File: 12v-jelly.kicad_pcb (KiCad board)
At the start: 4 copper layers, 46 x 68 mm, 30 parts, among them J1 PWR, J10 8, J3 1, J4 2, J5 3, J6 4, J7 5, J8 6, J9 7, Q1 DMP2022LSS-13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

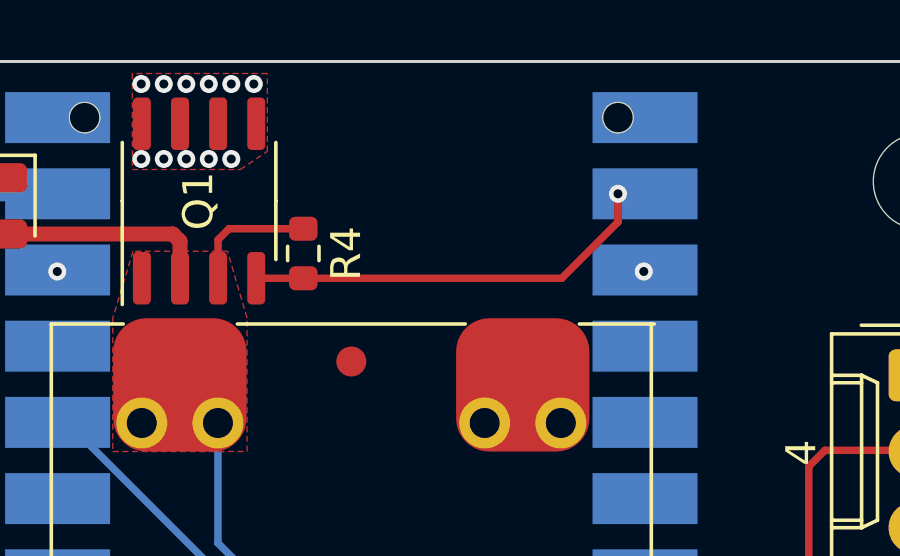
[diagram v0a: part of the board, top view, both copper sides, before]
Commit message: Driver NMOS
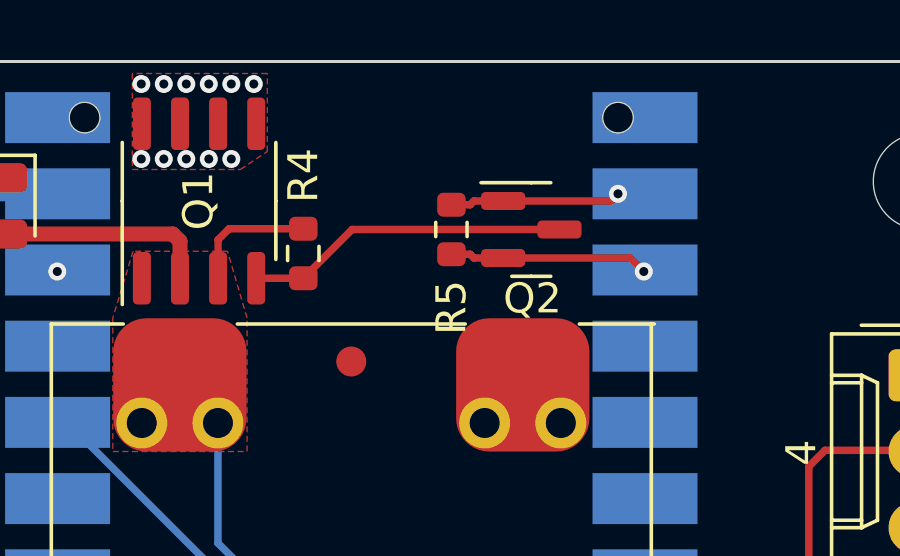
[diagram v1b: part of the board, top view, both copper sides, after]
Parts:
- added Q2: 2N7002, Package_TO_SOT_SMD:SOT-23, F.Cu at (86.0, 25.6)
- added R5: 10k, Resistor_SMD:R_0603_1608Metric, F.Cu at (83.3, 25.6)
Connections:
- Q1 pad 4: /LED_EN -> Net-(Q1-G)
- R4 pad 2: /LED_EN -> Net-(Q1-G)
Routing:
- net Net-(Q1-G): track 0.00 -> 10.8 mm
- net /LED_EN: track 13.8 -> 5.70 mm
- net GND: track 14.4 -> 21.0 mm
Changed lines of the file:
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@@
   (net 50 "/LED_EN")
   (net 51 "unconnected-(U2-GPIO0-Pad1)")
+  (net 52 "Net-(Q1-G)")
+  (footprint "Package_TO_SOT_SMD:SOT-23" (layer "F.Cu")
+    (at 86 25.6)
+    (descr "SOT, 3 Pin (https://www.jedec.org/system/files/docs/to-236h.pdf variant AB), generated with kicad-footprint-generator ipc_gullwing_generator.py")
+    (tags "SOT TO_SOT_SMD")
+    (property "Sheetfile" "12v-jelly.kicad_sch")
+    (property "Sheetname" "")
+    (property "ki_description" "0.115A Id, 60V Vds, N-Channel MOSFET, SOT-23")
+    (property "ki_keywords" "N-Channel Switching MOSFET")
+    (attr smd)
+    (fp_text reference "Q2" (at 0.0375 2.3) (layer "F.SilkS")
+        (effects (font (size 1 1) (thickness 0.15)))
+    )
+    (fp_text value "2N7002" (at 0 2.4) (layer "F.Fab")
+        (effects (font (size 1 1) (thickness 0.15)))
+    )
+    (fp_text user "${REFERENCE}" (at 0 0) (layer "F.Fab")
+        (effects (font (size 0.32 0.32) (thickness 0.05)))
+    )
+    (fp_line (start 0 -1.56) (end -1.675 -1.56)
+      (stroke (width 0.12) (type solid)) (layer "F.SilkS"))
+    (fp_line (start 0 -1.56) (end 0.65 -1.56)
+      (stroke (width 0.12) (type solid)) (layer "F.SilkS"))
+    (fp_line (start 0 1.56) (end -0.65 1.56)
+      (stroke (width 0.12) (type solid)) (layer "F.SilkS"))
+    (fp_line (start 0 1.56) (end 0.65 1.56)
+      (stroke (width 0.12) (type solid)) (layer "F.SilkS"))
+    (fp_line (start -1.92 -1.7) (end -1.92 1.7)
+      (stroke (width 0.05) (type solid)) (layer "F.CrtYd"))
+    (fp_line (start -1.92 1.7) (end 1.92 1.7)
+      (stroke (width 0.05) (type solid)) (layer "F.CrtYd"))
+    (fp_line (start 1.92 -1.7) (end -1.92 -1.7)
+      (stroke (width 0.05) (type solid)) (layer "F.CrtYd"))
+    (fp_line (start 1.92 1.7) (end 1.92 -1.7)
+      (stroke (width 0.05) (type solid)) (layer "F.CrtYd"))
+    (fp_line (start -0.65 -1.125) (end -0.325 -1.45)
+      (stroke (width 0.1) (type solid)) (layer "F.Fab"))
+    (fp_line (start -0.65 1.45) (end -0.65 -1.125)
+      (stroke (width 0.1) (type solid)) (layer "F.Fab"))
+    (fp_line (start -0.325 -1.45) (end 0.65 -1.45)
+      (stroke (width 0.1) (type solid)) (layer "F.Fab"))
+    (fp_line (start 0.65 -1.45) (end 0.65 1.45)
+      (stroke (width 0.1) (type solid)) (layer "F.Fab"))
+    (fp_line (start 0.65 1.45) (end -0.65 1.45)
+      (stroke (width 0.1) (type solid)) (layer "F.Fab"))
+    (pad "1" smd roundrect (at -0.9375 -0.95) (size 1.475 0.6) (layers "F.Cu" "F.Paste" "F.Mask") (roundrect_rratio 0.25)
+      (net 50 "/LED_EN") (pinfunction "G") (pintype "input"))
+    (pad "2" smd roundrect (at -0.9375 0.95) (size 1.475 0.6) (layers "F.Cu" "F.Paste" "F.Mask") (roundrect_rratio 0.25)
+      (net 2 "GND") (pinfunction "S") (pintype "passive"))
+    (pad "3" smd roundrect (at 0.9375 0) (size 1.475 0.6) (layers "F.Cu" "F.Paste" "F.Mask") (roundrect_rratio 0.25)
+      (net 52 "Net-(Q1-G)") (pinfunction "D") (pintype "passive"))
+    (model "${KICAD6_3DMODEL_DIR}/Package_TO_SOT_SMD.3dshapes/SOT-23.wrl"
+      (offset (xyz 0 0 0))
+      (scale (xyz 1 1 1))
+      (rotate (xyz 0 0 0))
+    )
+  )
   (footprint "Resistor_SMD:R_0603_1608Metric" (layer "F.Cu")
     (at 78.4 26.4 -90)
@@
     (property "ki_keywords" "R resistor")
     (attr smd)
-    (fp_text reference "R4" (at 0 -1.43 90) (layer "F.SilkS")
+    (fp_text reference "R4" (at -2.6 0 90) (layer "F.SilkS")
         (effects (font (size 1 1) (thickness 0.15)))
     )
@@
       (net 1 "+5V") (pintype "passive"))
     (pad "2" smd roundrect (at 0.825 0 270) (size 0.8 0.95) (layers "F.Cu" "F.Paste" "F.Mask") (roundrect_rratio 0.25)
-      (net 50 "/LED_EN") (pintype "passive"))
+      (net 52 "Net-(Q1-G)") (pintype "passive"))
     (model "${KICAD6_3DMODEL_DIR}/Resistor_SMD.3dshapes/R_0603_1608Metric.wrl"
       (offset (xyz 0 0 0))
@@
     )
   )
+  (footprint "Resistor_SMD:R_0603_1608Metric" (layer "F.Cu")
+    (at 83.3375 25.6 -90)
+    (descr "Resistor SMD 0603 (1608 Metric), square (rectangular) end terminal, IPC_7351 nominal, (Body size source: IPC-SM-782 page 72, https://www.pcb-3d.com/wordpress/wp-content/uploads/ipc-sm-782a_amendment_1_and_2.pdf), generated with kicad-footprint-generator")
+    (tags "resistor")
+    (property "Sheetfile" "12v-jelly.kicad_sch")
+    (property "Sheetname" "")
+    (property "ki_description" "Resistor, small symbol")
+    (property "ki_keywords" "R resistor")
+    (attr smd)
+    (fp_text reference "R5" (at 2.6 0 90) (layer "F.SilkS")
+        (effects (font (size 1 1) (thickness 0.15)))
+    )
+    (fp_text value "10k" (at 0 1.43 90) (layer "F.Fab")
+        (effects (font (size 1 1) (thickness 0.15)))
+    )
+    (fp_text user "${REFERENCE}" (at 0 0 90) (layer "F.Fab")
+        (effects (font (size 0.4 0.4) (thickness 0.06)))
+    )
+    (fp_line (start -0.237258 -0.5225) (end 0.237258 -0.5225)
+      (stroke (width 0.12) (type solid)) (layer "F.SilkS"))
+    (fp_line (start -0.237258 0.5225) (end 0.237258 0.5225)
+      (stroke (width 0.12) (type solid)) (layer "F.SilkS"))
+    (fp_line (start -1.48 -0.73) (end 1.48 -0.73)
+      (stroke (width 0.05) (type solid)) (layer "F.CrtYd"))
+    (fp_line (start -1.48 0.73) (end -1.48 -0.73)
+      (stroke (width 0.05) (type solid)) (layer "F.CrtYd"))
+    (fp_line (start 1.48 -0.73) (end 1.48 0.73)
+      (stroke (width 0.05) (type solid)) (layer "F.CrtYd"))
+    (fp_line (start 1.48 0.73) (end -1.48 0.73)
+      (stroke (width 0.05) (type solid)) (layer "F.CrtYd"))
+    (fp_line (start -0.8 -0.4125) (end 0.8 -0.4125)
+      (stroke (width 0.1) (type solid)) (layer "F.Fab"))
+    (fp_line (start -0.8 0.4125) (end -0.8 -0.4125)
+      (stroke (width 0.1) (type solid)) (layer "F.Fab"))
+    (fp_line (start 0.8 -0.4125) (end 0.8 0.4125)
+      (stroke (width 0.1) (type solid)) (layer "F.Fab"))
+    (fp_line (start 0.8 0.4125) (end -0.8 0.4125)
+      (stroke (width 0.1) (type solid)) (layer "F.Fab"))
+    (pad "1" smd roundrect (at -0.825 0 270) (size 0.8 0.95) (layers "F.Cu" "F.Paste" "F.Mask") (roundrect_rratio 0.25)
+      (net 50 "/LED_EN") (pintype "passive"))
+    (pad "2" smd roundrect (at 0.825 0 270) (size 0.8 0.95) (layers "F.Cu" "F.Paste" "F.Mask") (roundrect_rratio 0.25)
+      (net 2 "GND") (pintype "passive"))
+    (model "${KICAD6_3DMODEL_DIR}/Resistor_SMD.3dshapes/R_0603_1608Metric.wrl"
+      (offset (xyz 0 0 0))
+      (scale (xyz 1 1 1))
+      (rotate (xyz 0 0 0))
+    )
+  )
   (footprint "Fiducial:Fiducial_1mm_Mask2mm" (layer "F.Cu")
     (at 94 70)
@@
       (net 1 "+5V") (pinfunction "S") (pintype "passive"))
     (pad "4" smd roundrect (at -2.575 1.905 90) (size 1.75 0.6) (layers "F.Cu" "F.Paste" "F.Mask") (roundrect_rratio 0.25)
-      (net 50 "/LED_EN") (pinfunction "G") (pintype "input"))
+      (net 52 "Net-(Q1-G)") (pinfunction "G") (pintype "input"))
     (pad "5" smd roundrect (at 2.575 1.905 90) (size 1.75 0.6) (layers "F.Cu" "F.Paste" "F.Mask") (roundrect_rratio 0.25)
       (net 48 "LED_PWR") (pinfunction "D") (pintype "passive"))
@@
   (segment (start 94.25 46.13038) (end 94.25 75) (width 0.25) (layer "B.Cu") (net 1))
   (segment (start 91.61962 43.5) (end 94.25 46.13038) (width 0.25) (layer "B.Cu") (net 1))
+  (segment (start 83.3375 26.425) (end 83.9625 26.425) (width 0.25) (layer "F.Cu") (net 2))
   (segment (start 86 66.25) (end 86 67.2) (width 0.25) (layer "F.Cu") (net 2))
+  (segment (start 85.0625 26.55) (end 89.3 26.55) (width 0.25) (layer "F.Cu") (net 2))
   (segment (start 74.75 63.75) (end 75.53 63.75) (width 0.25) (layer "F.Cu") (net 2))
   (segment (start 80.975 83.525) (end 80 84.5) (width 0.25) (layer "F.Cu") (net 2))
+  (segment (start 83.9625 26.425) (end 84.0875 26.55) (width 0.25) (layer "F.Cu") (net 2))
   (segment (start 76 65.5) (end 75.555 65.055) (width 0.25) (layer "F.Cu") (net 2))
   (segment (start 75.53 63.75) (end 75.555 63.775) (width 0.25) (layer "F.Cu") (net 2))
@@
   (segment (start 80.975 81.815) (end 80.975 83.525) (width 0.25) (layer "F.Cu") (net 2))
   (segment (start 75.555 65.055) (end 75.555 63.775) (width 0.25) (layer "F.Cu") (net 2))
+  (segment (start 89.3 26.55) (end 89.75 27) (width 0.25) (layer "F.Cu") (net 2))
+  (segment (start 84.0875 26.55) (end 85.0625 26.55) (width 0.25) (layer "F.Cu") (net 2))
   (segment (start 80.635 65.885) (end 80.25 65.5) (width 0.25) (layer "F.Cu") (net 2))
   (via (at 70.2 27) (size 0.6) (drill 0.3) (layers "F.Cu" "B.Cu") (net 2))
@@
   (via (at 73 23.25) (size 0.6) (drill 0.3) (layers "F.Cu" "B.Cu") (free) (net 48))
   (via (at 74.5 20.75) (size 0.6) (drill 0.3) (layers "F.Cu" "B.Cu") (free) (net 48))
-  (segment (start 87.015 27.225) (end 88.89 25.35) (width 0.25) (layer "F.Cu") (net 50))
-  (segment (start 88.89 25.35) (end 88.89 24.41) (width 0.25) (layer "F.Cu") (net 50))
-  (segment (start 76.83 27.225) (end 87.015 27.225) (width 0.25) (layer "F.Cu") (net 50))
+  (segment (start 83.9625 24.775) (end 84.0875 24.65) (width 0.25) (layer "F.Cu") (net 50))
+  (segment (start 85.0625 24.65) (end 88.65 24.65) (width 0.25) (layer "F.Cu") (net 50))
+  (segment (start 83.3375 24.775) (end 83.9625 24.775) (width 0.25) (layer "F.Cu") (net 50))
+  (segment (start 84.0875 24.65) (end 85.0625 24.65) (width 0.25) (layer "F.Cu") (net 50))
+  (segment (start 88.65 24.65) (end 88.89 24.41) (width 0.25) (layer "F.Cu") (net 50))
   (via (at 88.89 24.41) (size 0.6) (drill 0.3) (layers "F.Cu" "B.Cu") (net 50))
+  (segment (start 76.83 27.225) (end 78.4 27.225) (width 0.25) (layer "F.Cu") (net 52))
+  (segment (start 86.9375 25.6) (end 80.025 25.6) (width 0.25) (layer "F.Cu") (net 52))
+  (segment (start 80.025 25.6) (end 78.4 27.225) (width 0.25) (layer "F.Cu") (net 52))
   (zone (net 48) (net_name "LED_PWR") (layer "F.Cu") (hatch edge 0.5)
     (priority 2)

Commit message: Oh gods the wires
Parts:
- moved D1 3.20 mm to (68.8, 28.0), turned to 90 degrees
- moved Q2 2.53 mm to (83.8, 26.8)
- moved R5 2.53 mm to (81.1, 26.8)
- moved R4 0.35 mm to (78.4, 26.8)
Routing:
- net GND: track 21.0 -> 305.6 mm, vias 9 -> 7
- net LED_PWR: track 13.7 -> 163.7 mm, vias 12 -> 0
- net +5V: track 85.4 -> 80.5 mm
- net Net-(J10-Pin_2): track 45.2 -> 40.6 mm, vias 0 -> 1
- net Net-(D1-K): track 4.95 -> 9.01 mm
- net /POT: track 55.8 -> 51.9 mm
- net Net-(J6-Pin_2): track 47.9 -> 44.1 mm, vias 0 -> 1
- net Net-(J7-Pin_2): track 47.6 -> 43.7 mm, vias 0 -> 1
- net +3V3: track 66.7 -> 63.3 mm
- net /LED_EN: track 5.70 -> 8.43 mm
- net Net-(Q1-G): track 10.8 -> 8.34 mm
- net Net-(J1-Pin_2): track 21.2 -> 18.9 mm
- net Net-(J1-Pin_1): track 21.2 -> 18.9 mm
- net Net-(J4-Pin_2): track 37.2 -> 39.3 mm, vias 0 -> 1
- net Net-(J9-Pin_2): track 36.1 -> 34.7 mm, vias 0 -> 1
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- removed copper zone on In2.Cu, net GND
- removed copper zone on In1.Cu, net LED_PWR

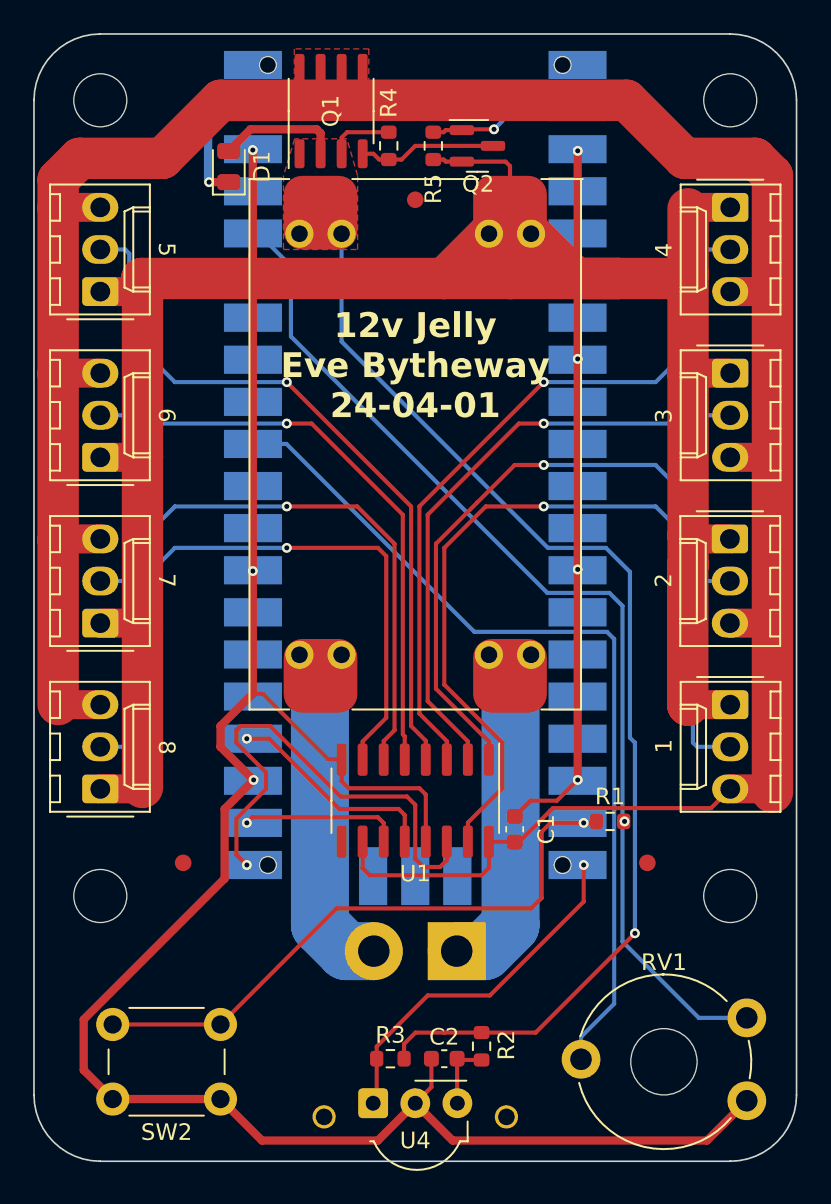
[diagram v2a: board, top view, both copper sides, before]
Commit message: More routing tweaks, and DRC fixes.
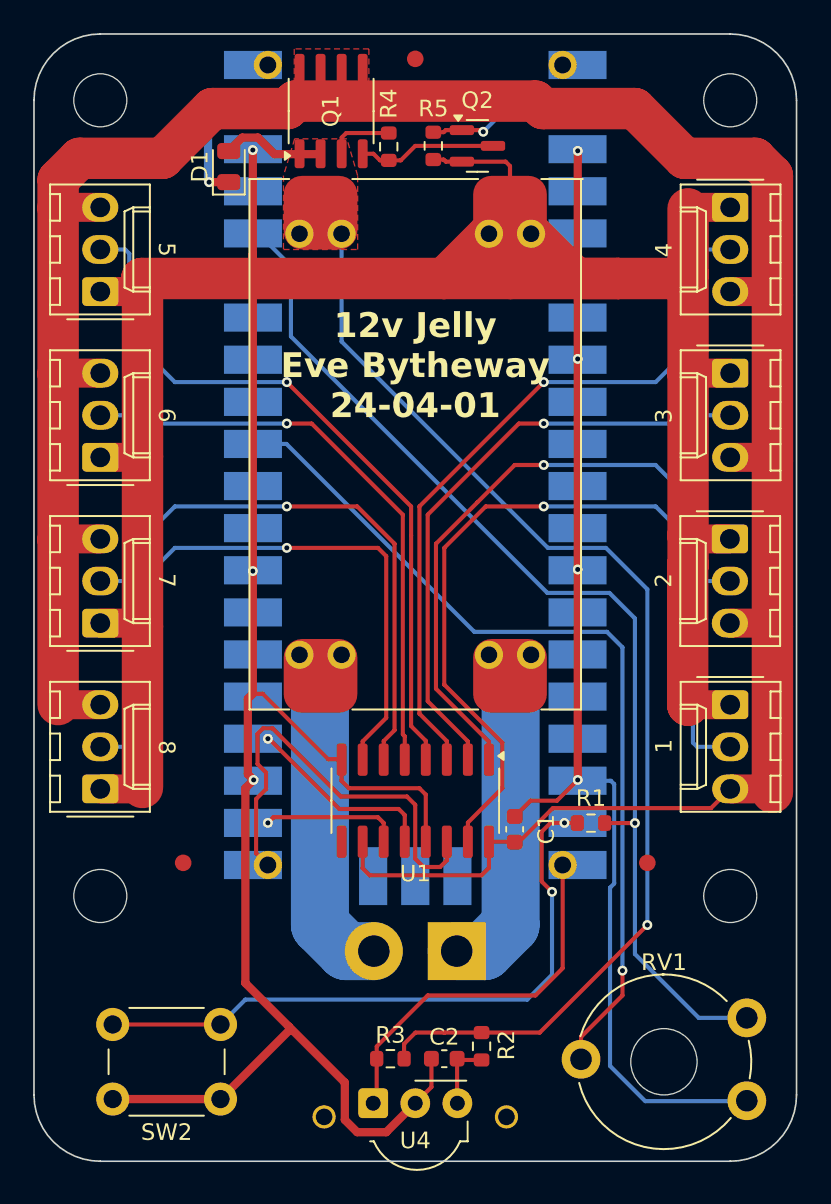
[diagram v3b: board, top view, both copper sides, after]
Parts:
- moved FID1 8.50 mm to (80.0, 21.5)
- moved R1 1.15 mm to (90.6, 67.6)
- moved R4 0.05 mm to (78.4, 26.8)
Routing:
- net GND: track 305.6 -> 308.1 mm
- net /DATA: track 29.4 -> 26.9 mm, vias 1 -> 0
- net /SW0: track 36.6 -> 39.0 mm, vias 1 -> 2
- net +3V3: track 63.3 -> 65.0 mm
- net /LATCH: track 13.0 -> 11.8 mm
- net /CLOCK: track 9.67 -> 8.40 mm
- net /IR: track 21.8 -> 22.9 mm, vias 1 -> 0
- net /POT: track 51.9 -> 52.4 mm, vias 0 -> 1
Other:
- copper layers 4 -> 2
